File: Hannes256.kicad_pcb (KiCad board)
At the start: 2 copper layers, 56.3 x 82 mm, 33 parts, among them J1 TED_SOCKET, J2 RAM_SELECTOR, J3 CONN_CS, U1 MOS_7360_TED, U10 41256, U11 41256, U12 41256, U13 41256, U14 41256, U2 GAL20V8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

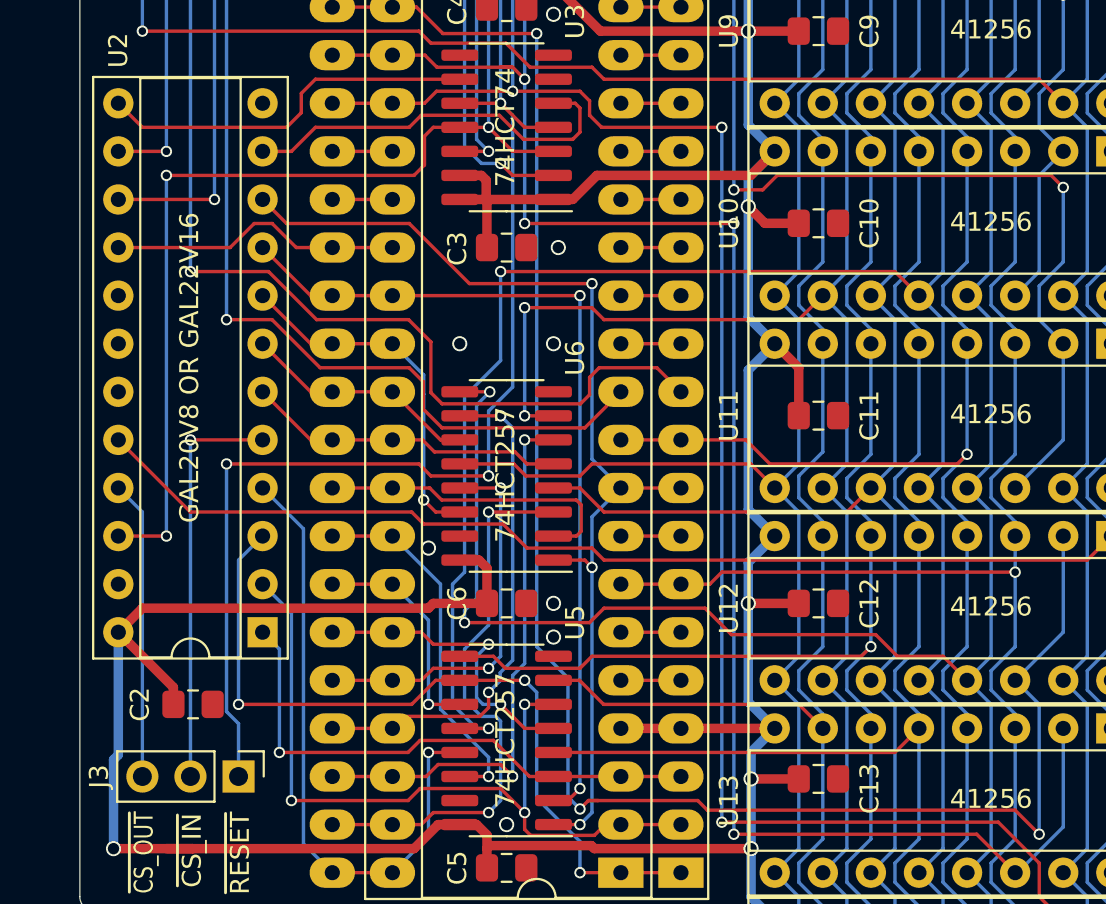
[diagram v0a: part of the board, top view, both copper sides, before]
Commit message: Bring R/W to the GAL We'll have to write an essay on this...
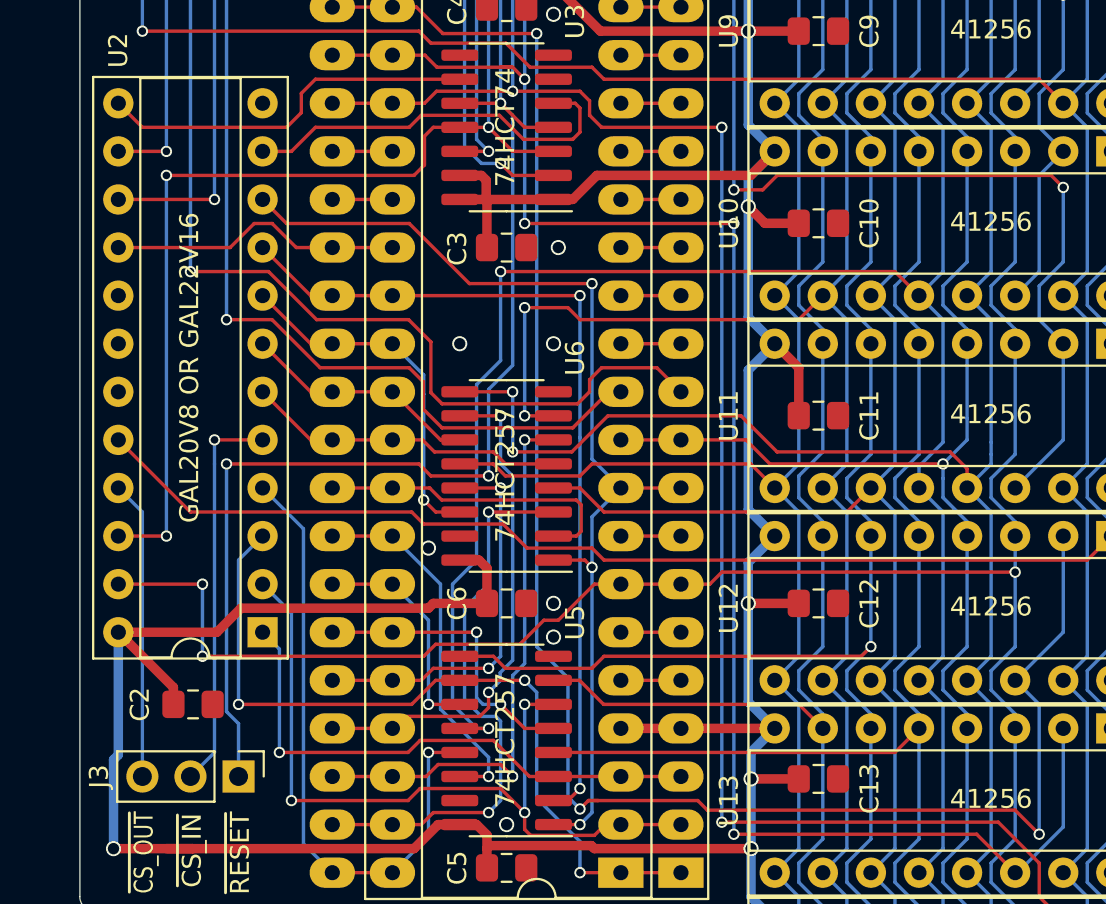
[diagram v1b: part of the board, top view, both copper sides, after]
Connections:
- U2 pad 17: (no net) -> Net-(U2-Pad17)
- U2 pad 18: (no net) -> Net-(U2-Pad18)
- U2 pad 19: (no net) -> Net-(U2-Pad19)
- U2 pad 23: (no net) -> R_~W
- U3 pad 6: (no net) -> Net-(U3-Pad6)
- U3 pad 8: (no net) -> Net-(U3-Pad8)
- U4 pad 6: (no net) -> Net-(U4-Pad6)
- U4 pad 8: (no net) -> Net-(U4-Pad8)
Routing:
- net R_~W: track 99.6 -> 131.5 mm, vias 1 -> 3
- net m6: track 121.3 -> 111.4 mm
- net ~RAS: track 97.5 -> 96.0 mm
- net ~CS_IN: track 21.6 -> 20.8 mm
- net a8: track 16.3 -> 15.8 mm

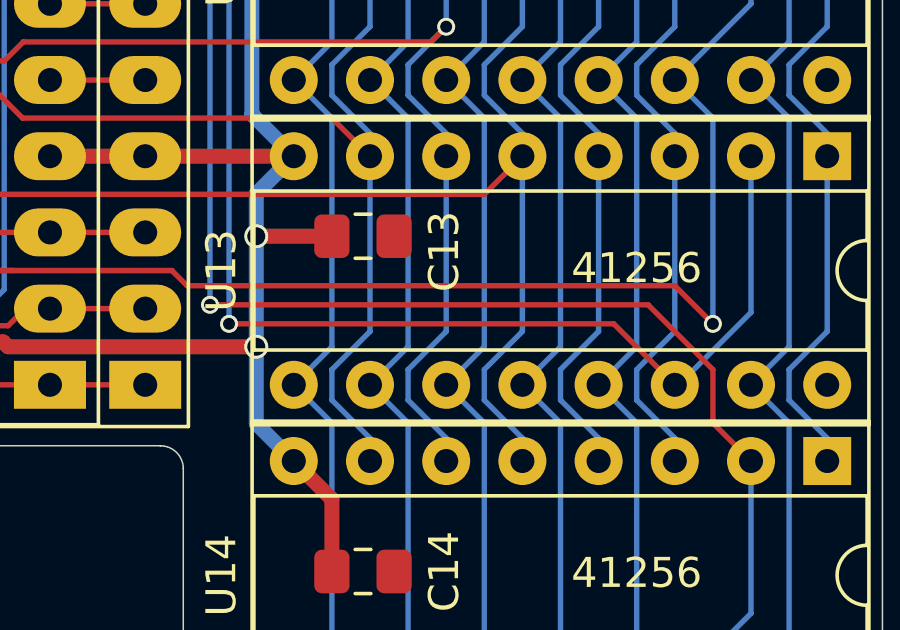
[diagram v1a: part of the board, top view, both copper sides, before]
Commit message: Center C13 within U13 The socket won't fit otherwise!
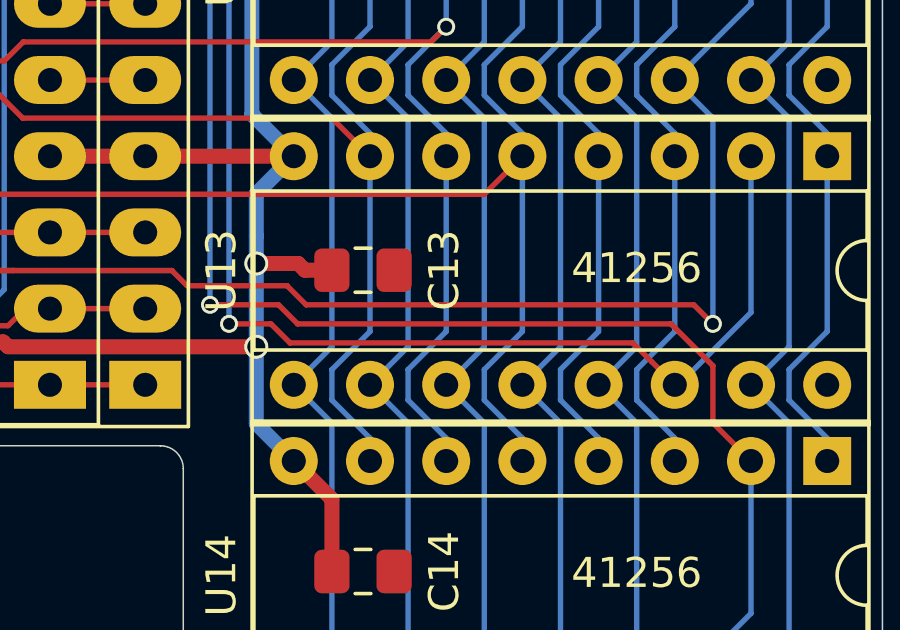
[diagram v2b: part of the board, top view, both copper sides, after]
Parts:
- moved C13 1.13 mm to (143.2, 133.1)
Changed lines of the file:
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@@
     (thickness 1.6)
     (drawings 30)
-    (tracks 1029)
+    (tracks 1038)
     (zones 0)
     (modules 33)
@@
     (31 B.Cu signal)
     (36 B.SilkS user hide)
-    (37 F.SilkS user hide)
+    (37 F.SilkS user)
     (38 B.Mask user hide)
     (39 F.Mask user hide)
@@
   )
   (module Capacitor_SMD:C_0805_2012Metric_Pad1.18x1.45mm_HandSolder (layer F.Cu)
-    (at 143.1505 131.953)
+    (at 143.1505 133.086)
     (descr "Capacitor SMD 0805 (2012 Metric), square (rectangular) end terminal, IPC_7351 nominal with elongated pad for handsoldering. (Body size source: IPC-SM-782 page 76, https://www.pcb-3d.com/wordpress/wp-content/uploads/ipc-sm-782a_amendment_1_and_2.pdf, https://docs.google.com/spreadsheets/d/1BsfQQcO9C6DZCsRaXUlFlo91Tg2WpOkGARC1WS5S8t0/edit?usp=sharing), generated with kicad-footprint-generator")
     (tags "capacitor handsolder")
     (attr smd)
-    (fp_text reference C13 (at 2.705 0.508 90) (layer F.SilkS)
+    (fp_text reference C13 (at 2.705 0 90) (layer F.SilkS)
       (effects (font (size 1 1) (thickness 0.15)))
     )
@@
   (segment (start 138.049 134.239) (end 138.049 97.536) (width 0.18) (layer B.Cu) (net 35))
   (via (at 138.049 97.536) (size 0.6) (drill 0.4) (layers F.Cu B.Cu) (net 35))
-  (segment (start 138.049 134.239) (end 152.654 134.239) (width 0.18) (layer F.Cu) (net 35))
-  (segment (start 152.654 134.239) (end 154.813 136.398) (width 0.18) (layer F.Cu) (net 35))
-  (segment (start 154.813 136.398) (end 154.813 138.176) (width 0.18) (layer F.Cu) (net 35))
-  (segment (start 154.813 138.176) (end 156.083 139.446) (width 0.18) (layer F.Cu) (net 35) (status 20))
   (segment (start 122.977757 95.631) (end 127 95.631) (width 0.18) (layer F.Cu) (net 35))
   (segment (start 122.342757 96.266) (end 122.977757 95.631) (width 0.18) (layer F.Cu) (net 35))
   (segment (start 120.65 96.266) (end 122.342757 96.266) (width 0.18) (layer F.Cu) (net 35) (status 10))
+  (segment (start 154.813 138.176) (end 156.083 139.446) (width 0.18) (layer F.Cu) (net 35))
+  (segment (start 154.813 136.271) (end 154.813 138.176) (width 0.18) (layer F.Cu) (net 35))
+  (segment (start 153.416 134.874) (end 154.813 136.271) (width 0.18) (layer F.Cu) (net 35))
+  (segment (start 140.97 134.874) (end 153.416 134.874) (width 0.18) (layer F.Cu) (net 35))
+  (segment (start 140.335 134.239) (end 140.97 134.874) (width 0.18) (layer F.Cu) (net 35))
+  (segment (start 138.049 134.239) (end 140.335 134.239) (width 0.18) (layer F.Cu) (net 35))
   (segment (start 117.475 93.726) (end 120.65 93.726) (width 0.18) (layer F.Cu) (net 36) (status 30))
   (segment (start 127.635 94.996) (end 127.635 87.376) (width 0.18) (layer B.Cu) (net 36))
@@
   (via (at 138.684 102.616) (size 0.6) (drill 0.4) (layers F.Cu B.Cu) (net 36))
   (segment (start 127.635 102.616) (end 138.684 102.616) (width 0.18) (layer F.Cu) (net 36))
-  (segment (start 151.511 134.874) (end 138.684 134.874) (width 0.18) (layer F.Cu) (net 36))
-  (segment (start 153.543 136.906) (end 151.511 134.874) (width 0.18) (layer F.Cu) (net 36) (status 10))
   (segment (start 138.684 102.616) (end 138.684 134.874) (width 0.18) (layer B.Cu) (net 36))
   (via (at 138.684 134.874) (size 0.6) (drill 0.4) (layers F.Cu B.Cu) (net 36))
@@
   (segment (start 122.3645 93.726) (end 122.9995 94.361) (width 0.18) (layer F.Cu) (net 36))
   (segment (start 120.65 93.726) (end 122.3645 93.726) (width 0.18) (layer F.Cu) (net 36) (status 10))
+  (segment (start 152.781 136.144) (end 153.543 136.906) (width 0.18) (layer F.Cu) (net 36))
+  (segment (start 152.146 135.509) (end 152.781 136.144) (width 0.18) (layer F.Cu) (net 36))
+  (segment (start 140.716 135.509) (end 152.146 135.509) (width 0.18) (layer F.Cu) (net 36))
+  (segment (start 140.081 134.874) (end 140.716 135.509) (width 0.18) (layer F.Cu) (net 36))
+  (segment (start 138.684 134.874) (end 140.081 134.874) (width 0.18) (layer F.Cu) (net 36))
   (segment (start 153.543 68.326) (end 153.543 74.168) (width 0.18) (layer B.Cu) (net 37) (status 10))
   (segment (start 153.543 74.168) (end 152.273 75.438) (width 0.18) (layer B.Cu) (net 37))
@@
   (segment (start 131.508498 133.096002) (end 131.000498 133.096002) (width 0.18) (layer F.Cu) (net 38))
   (segment (start 153.543 126.746) (end 154.813 128.016) (width 0.18) (layer B.Cu) (net 38) (status 10))
-  (segment (start 136.779002 133.096002) (end 137.287 133.604) (width 0.18) (layer F.Cu) (net 38))
-  (segment (start 131.508498 133.096002) (end 136.779002 133.096002) (width 0.18) (layer F.Cu) (net 38))
   (via (at 154.813 134.874) (size 0.6) (drill 0.4) (layers F.Cu B.Cu) (net 38))
-  (segment (start 153.543 133.604) (end 154.813 134.874) (width 0.18) (layer F.Cu) (net 38))
-  (segment (start 137.287 133.604) (end 153.543 133.604) (width 0.18) (layer F.Cu) (net 38))
   (segment (start 154.813 134.874) (end 154.813 128.016) (width 0.18) (layer B.Cu) (net 38))
   (segment (start 128.27 92.583) (end 128.27 124.968) (width 0.18) (layer B.Cu) (net 38))
@@
   (segment (start 129.921 132.905498) (end 130.079751 133.064249) (width 0.18) (layer B.Cu) (net 38))
   (segment (start 129.921 126.619) (end 129.921 132.905498) (width 0.18) (layer B.Cu) (net 38))
+  (segment (start 154.178 134.239) (end 154.813 134.874) (width 0.18) (layer F.Cu) (net 38))
+  (segment (start 141.25575 134.239) (end 154.178 134.239) (width 0.18) (layer F.Cu) (net 38))
+  (segment (start 140.62075 133.604) (end 141.25575 134.239) (width 0.18) (layer F.Cu) (net 38))
+  (segment (start 137.287 133.604) (end 140.62075 133.604) (width 0.18) (layer F.Cu) (net 38))
+  (segment (start 136.779002 133.096002) (end 137.287 133.604) (width 0.18) (layer F.Cu) (net 38))
+  (segment (start 131.508498 133.096002) (end 136.779002 133.096002) (width 0.18) (layer F.Cu) (net 38))
   (segment (start 156.083 114.046) (end 153.543 116.586) (width 0.18) (layer B.Cu) (net 39) (status 20))
   (segment (start 156.083 108.966) (end 156.083 114.046) (width 0.18) (layer B.Cu) (net 39) (status 10))
@@
   (segment (start 142.113 140.716) (end 140.843 139.446) (width 0.5) (layer F.Cu) (net 48) (status 20))
   (segment (start 142.113 143.129) (end 142.113 140.716) (width 0.5) (layer F.Cu) (net 48) (status 10))
-  (via (at 139.592999 131.953) (size 0.8) (drill 0.6) (layers F.Cu B.Cu) (net 48))
-  (segment (start 139.612998 131.953) (end 139.592999 131.933001) (width 0.5) (layer F.Cu) (net 48))
-  (segment (start 142.113 131.953) (end 139.612998 131.953) (width 0.5) (layer F.Cu) (net 48) (status 10))
-  (segment (start 139.592999 131.933001) (end 139.592999 138.195999) (width 0.5) (layer B.Cu) (net 48))
   (segment (start 139.592999 130.536001) (end 139.592999 131.933001) (width 0.5) (layer B.Cu) (net 48))
   (via (at 139.446 122.682) (size 0.8) (drill 0.6) (layers F.Cu B.Cu) (net 48))
@@
   (segment (start 106.172 124.206) (end 111.379 124.206) (width 0.5) (layer F.Cu) (net 48))
   (segment (start 122.555 122.936) (end 112.649 122.936) (width 0.5) (layer F.Cu) (net 48))
+  (segment (start 142.113 133.086) (end 141.214 133.086) (width 0.5) (layer F.Cu) (net 48))
+  (via (at 139.592999 132.861999) (size 0.8) (drill 0.6) (layers F.Cu B.Cu) (net 48))
+  (segment (start 140.989999 132.861999) (end 139.592999 132.861999) (width 0.5) (layer F.Cu) (net 48))
+  (segment (start 141.214 133.086) (end 140.989999 132.861999) (width 0.5) (layer F.Cu) (net 48))
+  (segment (start 139.592999 132.861999) (end 139.592999 138.195999) (width 0.5) (layer B.Cu) (net 48))
+  (segment (start 139.592999 131.933001) (end 139.592999 132.861999) (width 0.5) (layer B.Cu) (net 48))
   (segment (start 132.715 116.586) (end 135.89 116.586) (width 0.18) (layer F.Cu) (net 49) (status 30))
   (segment (start 130.81 120.396) (end 131.191 120.777) (width 0.18) (layer F.Cu) (net 49))

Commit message: Cosmetics
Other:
- board text added: "256kB RAM Expansion for Commodore 16 Based on work by Hannes and Solder/Synergy"
- board text added: "ON C16: - ~CS_OUT~ IS PIN 10 OF U11 - ~CS_IN~ IS *LIFTED* PIN 16 OF U16 - ~RESET~ IS PIN 2 OF U9 OR PIN 40 OF U2 ON +4 IF YOU'RE SMART ENOUGH TO FIT THE BOARD, I'M SURE YOU CAN ALSO FIGURE OUT THE PINS :)"
- board text added: "V2"
- board text removed: "256k RAM Expansion for Commodore 16 Based on work by Hannes and Solder/Synergy"
- board text removed: "ON C16: - ~CS_OUT~ IS PIN 10 OF U11 - ~CS_IN~ IS *LIFTED* PIN 16 OF U16 - ~RESET~ IS PIN 2 OF U9 OR PIN 40 OF U2 ON +4 IF YOU'RE SMART ENOUGH TO FIT THE BOARD, YOU CAN ALSO FIGURE OUT THE PINS"
- board text removed: "V1"
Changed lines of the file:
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@@
     (0 F.Cu signal)
     (31 B.Cu signal)
-    (36 B.SilkS user hide)
+    (36 B.SilkS user)
     (37 F.SilkS user)
     (38 B.Mask user hide)
@@
     (effects (font (size 0.9 0.9) (thickness 0.15)) (justify right mirror))
   )
-  (gr_text "256k RAM Expansion for Commodore 16\nBased on work by Hannes and Solder/Synergy" (at 109.9245 110.231 90) (layer B.SilkS)
+  (gr_text "256kB RAM Expansion for Commodore 16\nBased on work by Hannes and Solder/Synergy" (at 109.9245 110.231 90) (layer B.SilkS)
     (effects (font (size 1 1) (thickness 0.15)) (justify mirror))
   )
-  (gr_text V1 (at 105.664 137.287 90) (layer B.SilkS)
+  (gr_text V2 (at 105.664 137.287 90) (layer B.SilkS)
     (effects (font (size 1 1) (thickness 0.15)) (justify mirror))
   )
-  (gr_text "ON C16:\n- ~CS_OUT~ IS PIN 10 OF U11\n- ~CS_IN~ IS *LIFTED* PIN 16 OF U16\n- ~RESET~ IS PIN 2 OF U9 OR PIN 40 OF U2\nON +4 IF YOU'RE SMART ENOUGH TO FIT THE BOARD,\nYOU CAN ALSO FIGURE OUT THE PINS" (at 126.492 80.226 90) (layer B.SilkS)
+  (gr_text "ON C16:\n- ~CS_OUT~ IS PIN 10 OF U11\n- ~CS_IN~ IS *LIFTED* PIN 16 OF U16\n- ~RESET~ IS PIN 2 OF U9 OR PIN 40 OF U2\nON +4 IF YOU'RE SMART ENOUGH TO FIT THE BOARD,\nI'M SURE YOU CAN ALSO FIGURE OUT THE PINS :)" (at 126.492 80.226 90) (layer B.SilkS)
     (effects (font (size 0.9 0.9) (thickness 0.14)) (justify left mirror))
   )
@@
   (segment (start 148.463 108.204) (end 148.463 108.966) (width 0.18) (layer B.Cu) (net 57) (status 30))
   (segment (start 147.193 106.934) (end 148.463 108.204) (width 0.18) (layer B.Cu) (net 57) (status 20))
-  (segment (start 148.463 108.966) (end 148.463 114.808) (width 0.18) (layer B.Cu) (net 57) (status 10))
-  (segment (start 148.463 114.808) (end 147.193 116.078) (width 0.18) (layer B.Cu) (net 57))
-  (segment (start 147.193 116.078) (end 147.193 117.094) (width 0.18) (layer B.Cu) (net 57))
-  (segment (start 148.463 118.364) (end 148.463 119.126) (width 0.18) (layer B.Cu) (net 57) (status 30))
-  (segment (start 147.193 117.094) (end 148.463 118.364) (width 0.18) (layer B.Cu) (net 57) (status 20))
   (segment (start 148.463 128.524) (end 148.463 129.286) (width 0.18) (layer B.Cu) (net 57) (status 30))
   (segment (start 147.193 127.254) (end 148.463 128.524) (width 0.18) (layer B.Cu) (net 57) (status 20))
@@
   (segment (start 129.1575 130.556) (end 147.193 130.556) (width 0.18) (layer F.Cu) (net 57) (status 10))
   (segment (start 147.193 130.556) (end 148.463 129.286) (width 0.18) (layer F.Cu) (net 57) (status 20))
+  (segment (start 147.193 117.094) (end 148.463 118.364) (width 0.18) (layer B.Cu) (net 57))
+  (segment (start 147.193 116.0145) (end 147.193 117.094) (width 0.18) (layer B.Cu) (net 57))
+  (segment (start 148.463 118.364) (end 148.463 119.126) (width 0.18) (layer B.Cu) (net 57))
+  (segment (start 148.463 114.7445) (end 147.193 116.0145) (width 0.18) (layer B.Cu) (net 57))
+  (segment (start 148.463 108.966) (end 148.463 114.7445) (width 0.18) (layer B.Cu) (net 57))
   (segment (start 145.923 75.946) (end 147.193 77.216) (width 0.18) (layer B.Cu) (net 58) (status 10))
   (segment (start 147.193 84.836) (end 145.923 86.106) (width 0.18) (layer B.Cu) (net 58) (status 20))
